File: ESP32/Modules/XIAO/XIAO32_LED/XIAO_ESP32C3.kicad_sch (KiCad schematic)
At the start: 3 parts, among them U1 XIAO-ESP32-C3-SMD

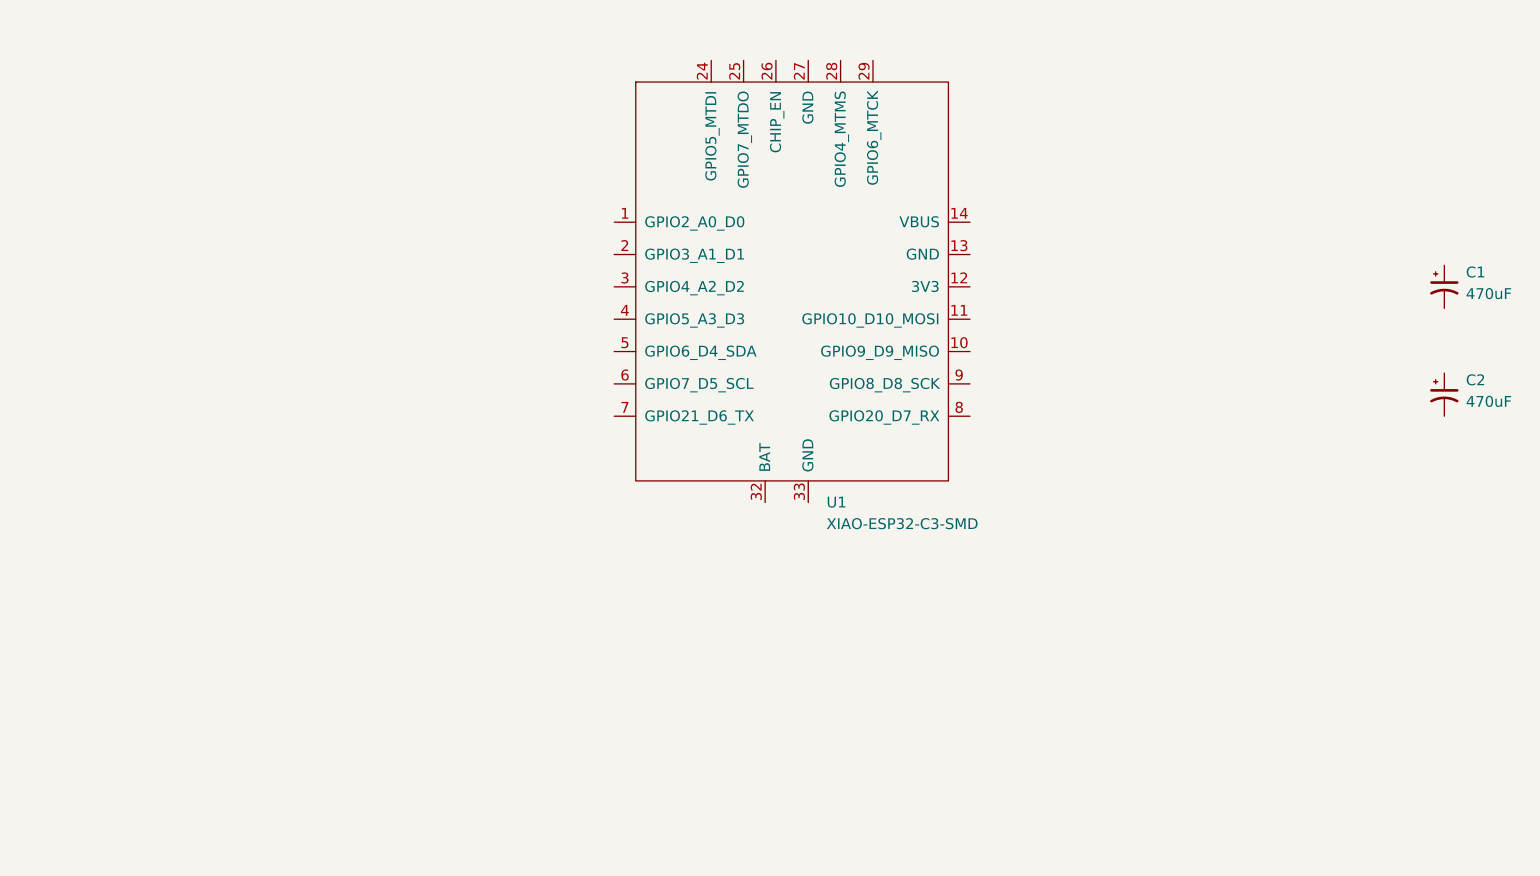
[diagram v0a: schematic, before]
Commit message: XIAO32_LED: MCU wired up
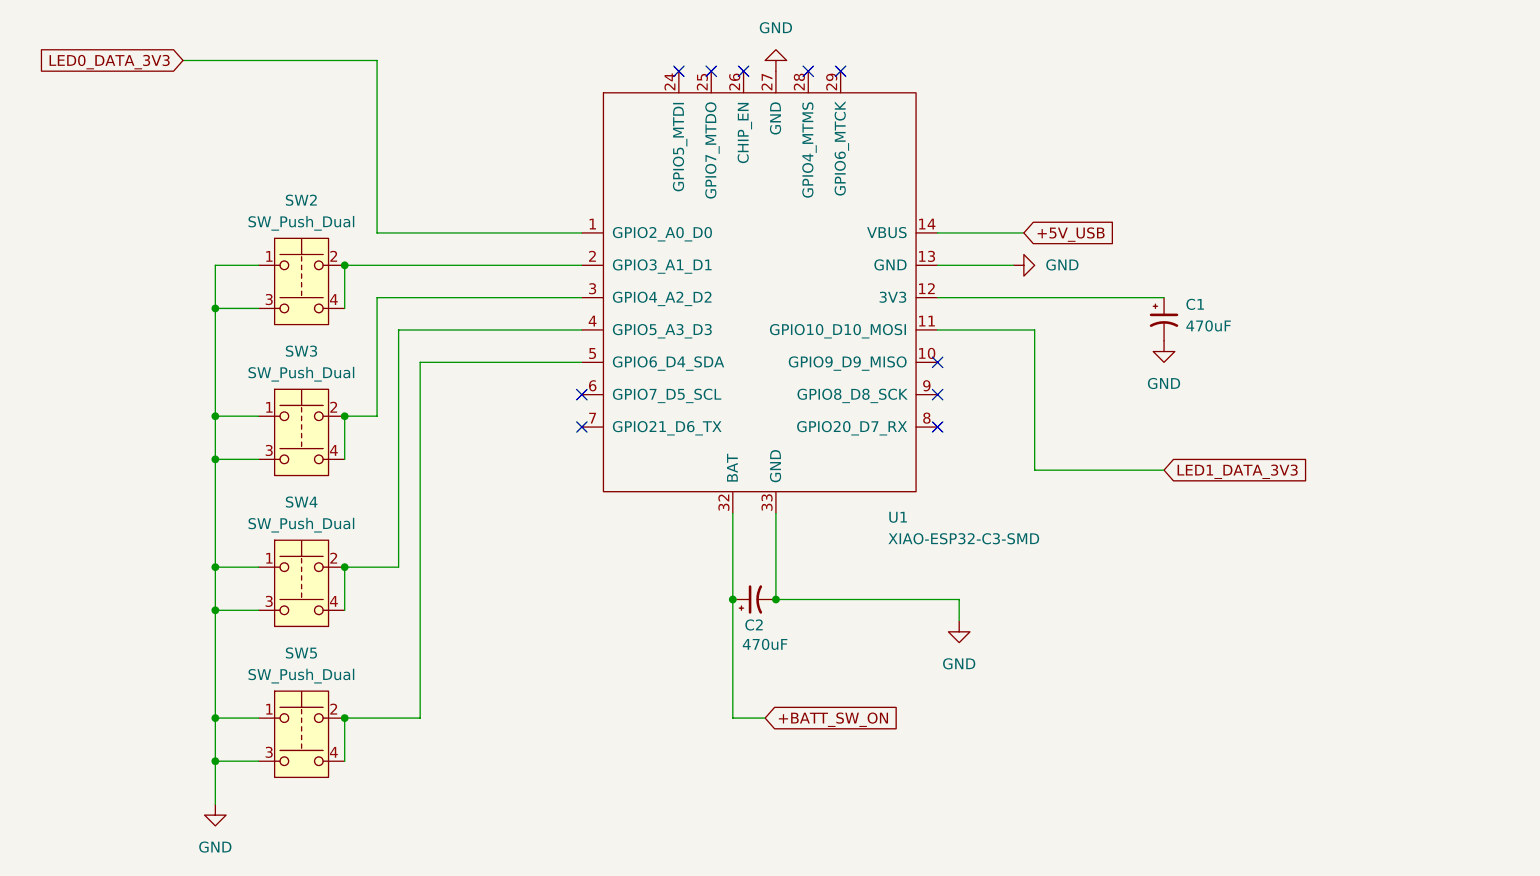
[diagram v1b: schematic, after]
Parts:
- added SW2, SW3, SW4, SW5: SW_Push_Dual, symbol Switch:SW_Push_Dual
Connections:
- net +BATT_SW_ON: now reaches C2.1
- net +BATT_SW_ON: now also U1.32 (BAT)
- net GND: now reaches C2.2
- net GND: now also C1.2, U1.13 (GND), U1.27 (GND), U1.33 (GND), SW2.1, SW2.3, SW3.1, SW3.3, SW4.1, SW4.3, SW5.1, SW5.3
- net LED0_DATA_3V3: now reaches U1.1 (GPIO2_A0_D0)
- net LED1_DATA_3V3: now reaches U1.11 (GPIO10_D10_MOSI)
- net at U1.12 (3V3): now also C1.1
- net +5V_USB: now reaches U1.14 (VBUS)
- net at U1.2 (GPIO3_A1_D1): now also SW2.2, SW2.4
- net at U1.3 (GPIO4_A2_D2): now also SW3.2, SW3.4
- net at U1.4 (GPIO5_A3_D3): now also SW4.2, SW4.4
- net at U1.5 (GPIO6_D4_SDA): now also SW5.2, SW5.4
- no-connect marks 0 -> 10
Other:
- moved on the sheet: C1, C2, U1

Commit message: XIAO32_LED: Convert sch to hierarchical pins
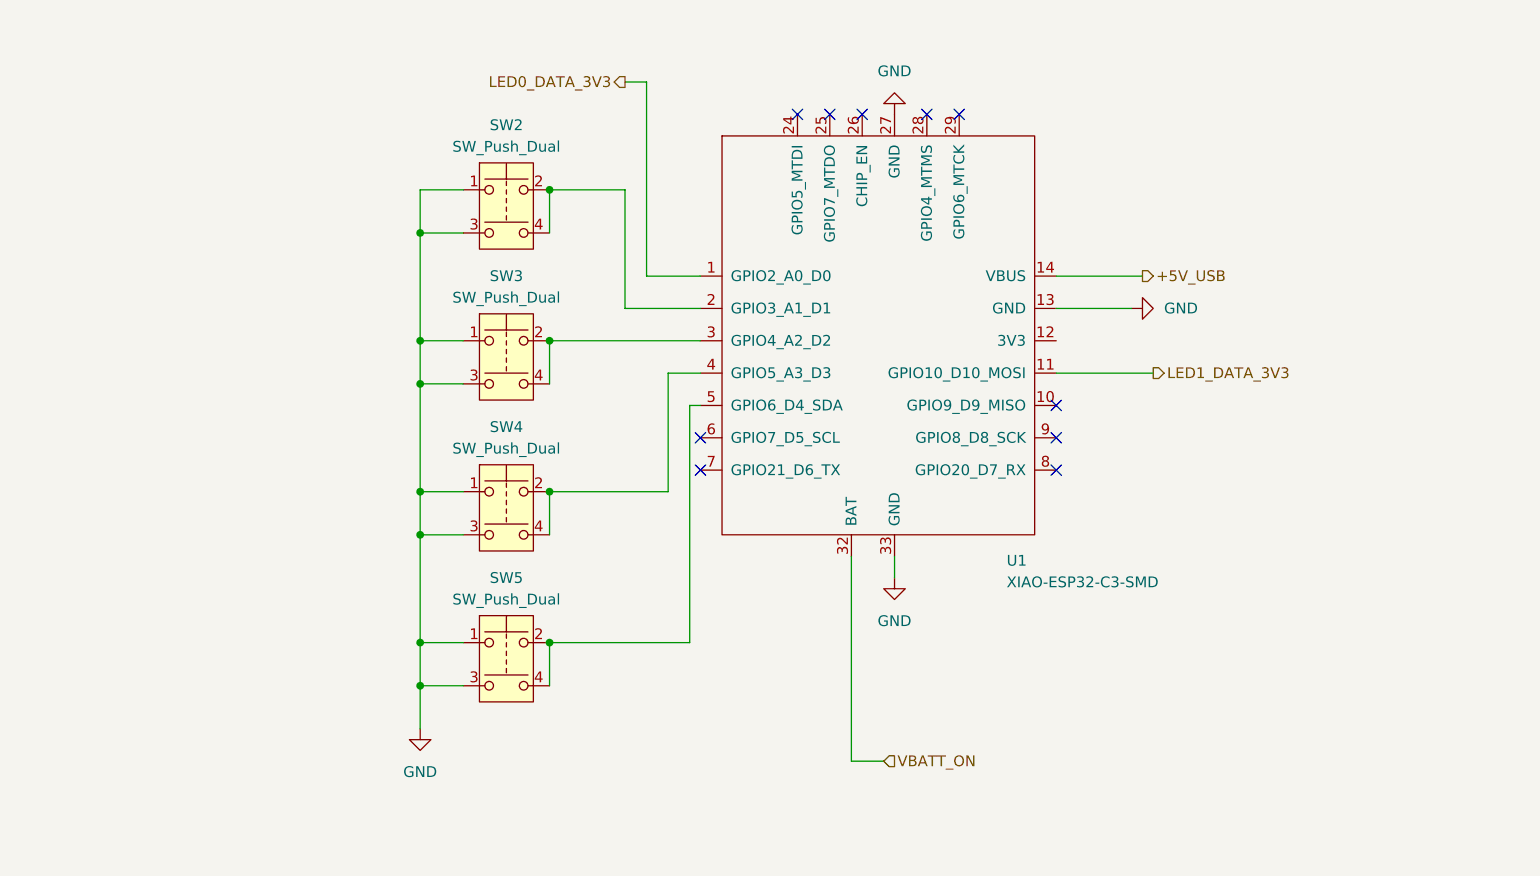
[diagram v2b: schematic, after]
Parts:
- removed C1, C2: 470uF, symbol Device:C_Polarized_Small_US
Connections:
- net +BATT_SW_ON renamed VBATT_ON
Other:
- moved on the sheet: SW2, SW3, SW4, SW5, U1
